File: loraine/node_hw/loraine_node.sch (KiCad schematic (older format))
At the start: 41 parts, among them CON1 BARREL_JACK, IC1 ATTINY2313A-S, P1 MOLEX, P2 MOLEX, P3 SOLDER_PAD, P4 ICSP, P5 OUTPUTS, P6 BUS, P7 BUS_THRU, Q1 BD679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

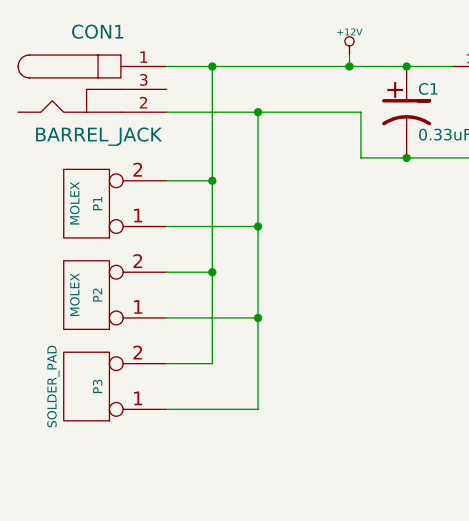
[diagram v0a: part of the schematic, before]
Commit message: Added locking 2-way MOLEX headers
MOLEX part 22-23-2021 for header = farnell 1462926
MOLEX part 22-01-3027 for receptacle = farnell 1462825
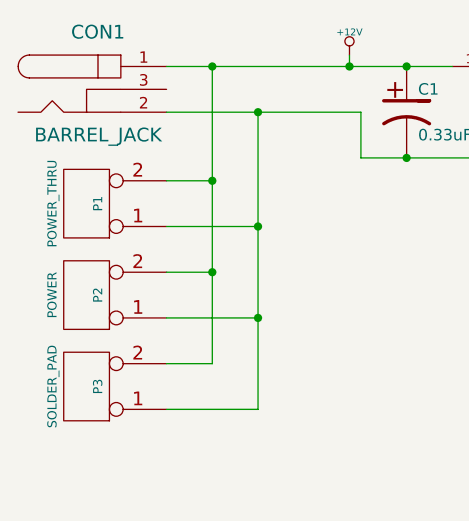
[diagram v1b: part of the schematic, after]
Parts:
- P1: value MOLEX -> POWER_THRU
- P2: value MOLEX -> POWER
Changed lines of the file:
@@
 P 1050 1750
 F 0 "P1" V 1000 1750 40  0000 C CNN
-F 1 "MOLEX" V 1100 1750 40  0000 C CNN
+F 1 "POWER_THRU" V 1200 1750 40  0000 C CNN
 F 2 "" H 1050 1750 60  0000 C CNN
 F 3 "" H 1050 1750 60  0000 C CNN
@@
 P 1050 2150
 F 0 "P2" V 1000 2150 40  0000 C CNN
-F 1 "MOLEX" V 1100 2150 40  0000 C CNN
+F 1 "POWER" V 1200 2150 40  0000 C CNN
 F 2 "" H 1050 2150 60  0000 C CNN
 F 3 "" H 1050 2150 60  0000 C CNN
